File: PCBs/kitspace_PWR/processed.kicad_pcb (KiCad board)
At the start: 2 copper layers, 26.7 x 53.3 mm, 19 parts, among them J1 Screw_Terminal_01x04, J2 Conn_01x01, J3 Conn_01x02, J5 Conn_01x01, Q1 TIC206, U1 MOC3021M, U2 4N25, U3 NodeMCU1.0(ESP-12E)

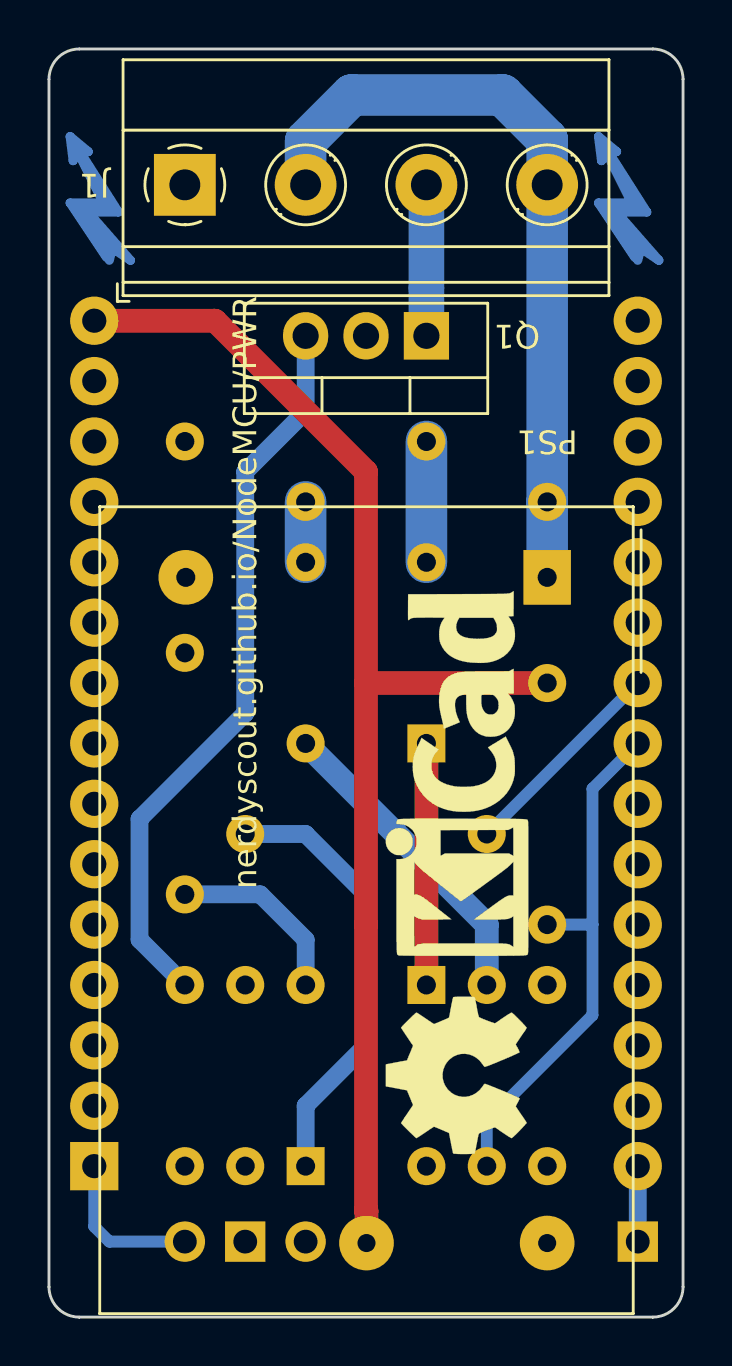
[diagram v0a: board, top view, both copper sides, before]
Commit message: recheck all circuits and clean up fill zone by rerouting the nets using freerouting and manually
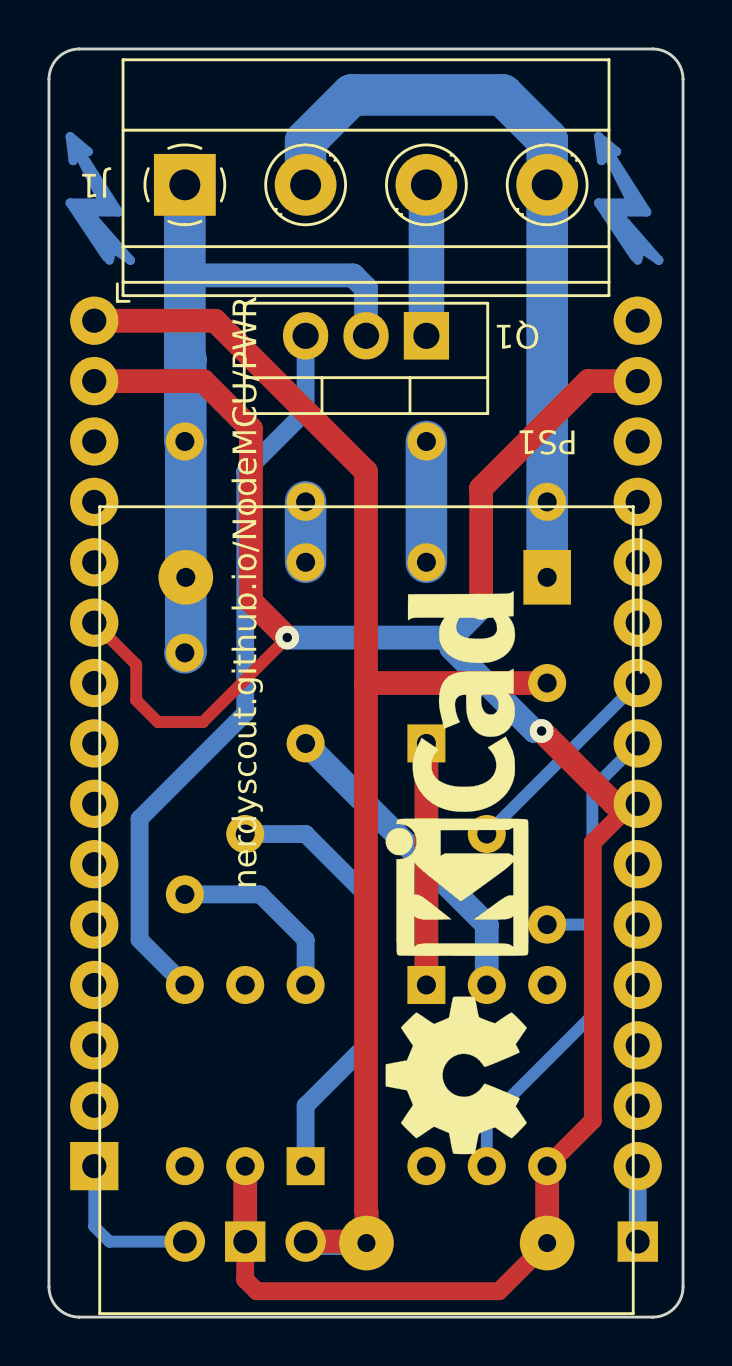
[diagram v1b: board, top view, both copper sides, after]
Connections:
- J1 pad 1: (no net) -> VAC
- J3 pad 1: (no net) -> GND
- J5 pad 1: (no net) -> +5V
- PS1 pad 2: (no net) -> VAC
- PS1 pad 3: (no net) -> GND
- Q1 pad 2: (no net) -> VAC
- R1 pad 1: (no net) -> VAC
- R2 pad 1: (no net) -> VAC
- U1 pad 2: (no net) -> GND
- U2 pad 4: (no net) -> GND
- U3 pad 10: (no net) -> GND
- U3 pad 14: (no net) -> GND
- U3 pad 17: (no net) -> GND
- U3 pad 24: (no net) -> GND
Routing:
- net GND: track 0.00 -> 100.9 mm, vias 0 -> 3
- net VAC: track 0.00 -> 33.1 mm
- net +5V: track 54.1 -> 59.3 mm
